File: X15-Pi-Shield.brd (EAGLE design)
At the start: 100 x 80 mm, 76 parts, among them J1 T2I, J2 T2I, J3 DF13-4P-1.25DSA, J4 T2I, J5 DF13-4P-1.25DSA, J6 DF13-4P-1.25DSA, Q1 220mA/50V/3.5Ω, Q2 2.5A/30V/105mΩ, Q3 220mA/50V/3.5Ω, Q4 220mA/50V/3.5Ω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

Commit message: 2nd try
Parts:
- removed C8: 150uF, CAP, Tantalum 150 uF - Kemet 2917 T491:2917(7343-31-METRIC)
- added C14: 150uF, X15-Pi-Shield-Parts:2917(7343-31-METRIC)
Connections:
- net GND: now also C14.-; no longer C8.-
- net PI_POWER: now also C14.+; no longer C8.+
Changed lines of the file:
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@@
 <attribute name="VALUE" x="-17.78" y="-386.842" size="0.6096" layer="27" font="vector" ratio="20" align="top-center"/>
-</element>
-<element name="C8" library="CAP, Tantalum 150 uF - Kemet 2917 T491" package="2917(7343-31-METRIC)" package3d_urn="urn:adsk.eagle:package:25131320/3" value="150uF" x="-13.97" y="-392.43" smashed="yes">
-<attribute name="NAME" x="-13.97" y="-389.89" size="1.27" layer="25" align="bottom-center"/>
-<attribute name="VALUE" x="-13.97" y="-394.97" size="1.27" layer="27" align="top-center"/>
 </element>
 <element name="J3" library="X15-Pi-Shield-Parts" package="DF13-4P-1.25DSA" value="DF13-4P-1.25DSA" x="-25.4" y="-391.16" smashed="yes">
@@
 <attribute name="VALUE" x="-76.2" y="-550.672" size="0.6096" layer="27" font="vector" ratio="20" align="top-center"/>
 </element>
+<element name="C14" library="X15-Pi-Shield-Parts" package="2917(7343-31-METRIC)" package3d_urn="urn:adsk.eagle:package:25131320/3" value="150uF" x="-72.39" y="-556.26" smashed="yes">
+<attribute name="NAME" x="-72.39" y="-553.72" size="1.27" layer="25" align="bottom-center"/>
+<attribute name="VALUE" x="-72.39" y="-558.8" size="1.27" layer="27" align="top-center"/>
+</element>
 </elements>
 <signals>
@@
 <contactref element="U$5" pad="GND"/>
 <contactref element="C7" pad="2"/>
-<contactref element="C8" pad="-"/>
 <contactref element="J3" pad="4"/>
 <contactref element="J5" pad="4"/>
@@
 <contactref element="U$6" pad="6"/>
 <contactref element="U$6" pad="10"/>
-<contactref element="C9" pad="-"/>
-<contactref element="U1" pad="8"/>
 <contactref element="D4" pad="C"/>
 <contactref element="D3" pad="C"/>
@@
 <contactref element="J15" pad="1"/>
 <contactref element="D5" pad="C"/>
-<contactref element="Q3" pad="2"/>
-<contactref element="U$7" pad="2"/>
 <contactref element="C10" pad="2"/>
 <contactref element="U$8" pad="11"/>
@@
 <contactref element="C12" pad="2"/>
 <contactref element="C13" pad="2"/>
+<contactref element="U1" pad="8"/>
+<contactref element="C9" pad="-"/>
+<contactref element="Q3" pad="2"/>
+<contactref element="U$7" pad="2"/>
+<contactref element="C14" pad="-"/>
 <wire x1="4.5466" y1="-262.4582" x2="12.1666" y2="-262.4582" width="0" layer="19" extent="1-1"/>
 <wire x1="-0.5334" y1="-264.9982" x2="4.5466" y2="-262.4582" width="0" layer="19" extent="1-1"/>
@@
 <wire x1="-6.985" y1="-361.95" x2="-6.35" y2="-337.82" width="0" layer="19" extent="1-1"/>
 <wire x1="-16.93" y1="-370.84" x2="-6.985" y2="-361.95" width="0" layer="19" extent="1-1"/>
-<wire x1="-10.75" y1="-392.43" x2="-16.93" y2="-370.84" width="0" layer="19" extent="1-1"/>
-<wire x1="-27.275" y1="-391.16" x2="-10.75" y2="-392.43" width="0" layer="19" extent="1-1"/>
+<wire x1="-27.275" y1="-391.16" x2="-16.93" y2="-370.84" width="0" layer="19" extent="1-1"/>
 <wire x1="-36.165" y1="-391.16" x2="-27.275" y2="-391.16" width="0" layer="19" extent="1-1"/>
 <wire x1="-45.055" y1="-391.16" x2="-36.165" y2="-391.16" width="0" layer="19" extent="1-1"/>
@@
 <wire x1="-75.35" y1="-518.16" x2="-71.4756" y2="-512.7498" width="0" layer="19" extent="1-1"/>
 <wire x1="-75.35" y1="-549.91" x2="-75.35" y2="-518.16" width="0" layer="19" extent="1-1"/>
+<wire x1="-69.17" y1="-556.26" x2="-75.35" y2="-549.91" width="0" layer="19" extent="1-1"/>
 <wire x1="-4.95" y1="-181.35" x2="-5.6134" y2="-262.4582" width="0" layer="19" extent="1-1"/>
 <wire x1="-19.05" y1="-166.37" x2="-4.95" y2="-181.35" width="0" layer="19" extent="1-1"/>
@@
 <contactref element="U$4" pad="2"/>
 <contactref element="R14" pad="2"/>
-<contactref element="C8" pad="+"/>
 <contactref element="R13" pad="2"/>
-<wire x1="-16.93" y1="-386.08" x2="-17.19" y2="-392.43" width="0" layer="19" extent="1-1"/>
+<contactref element="C14" pad="+"/>
 <wire x1="-16.93" y1="-382.27" x2="-16.93" y2="-386.08" width="0" layer="19" extent="1-1"/>
 <wire x1="-10.6934" y1="-262.4582" x2="-16.93" y2="-382.27" width="0" layer="19" extent="1-1"/>
 <wire x1="-8.1534" y1="-262.4582" x2="-10.6934" y2="-262.4582" width="0" layer="19" extent="1-1"/>
+<wire x1="-75.61" y1="-556.26" x2="-16.93" y2="-386.08" width="0" layer="19" extent="1-1"/>
 </signal>
 <signal name="SCL/3.6C">

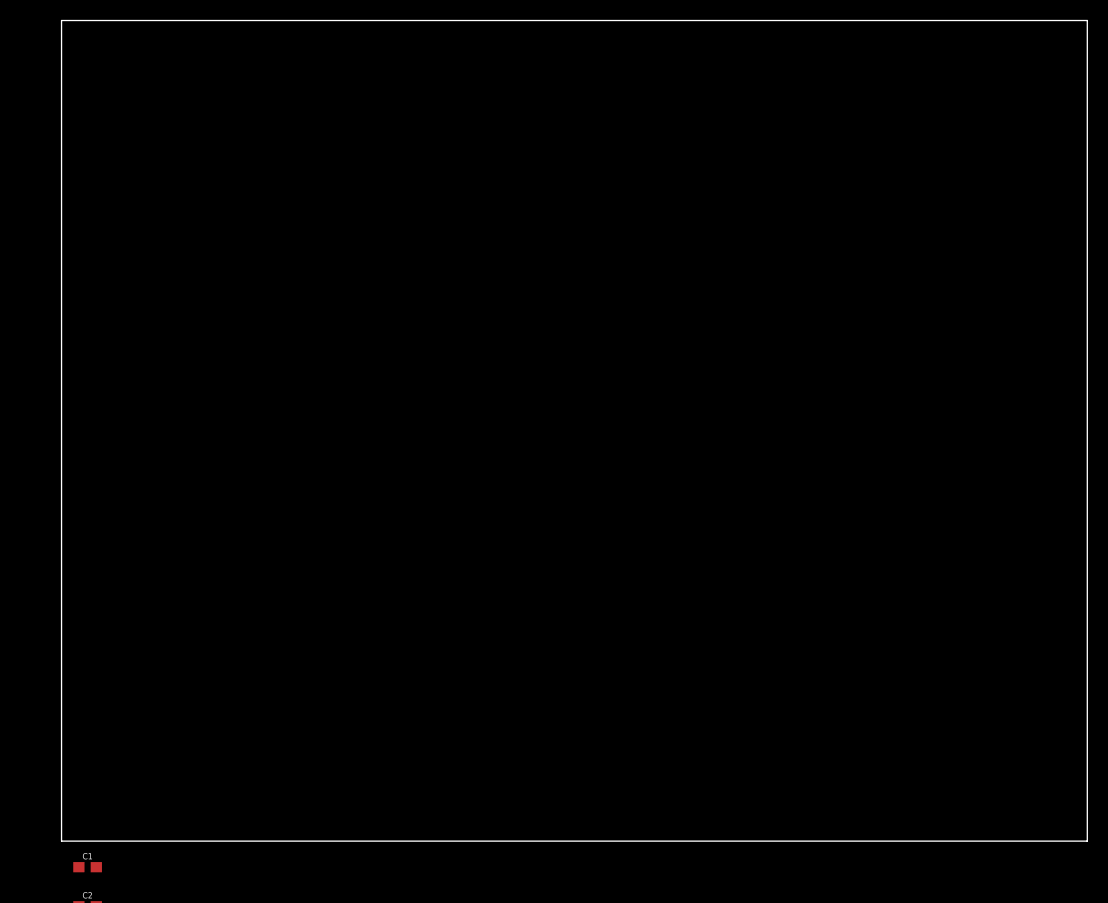
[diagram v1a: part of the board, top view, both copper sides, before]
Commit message: Board Dimensions
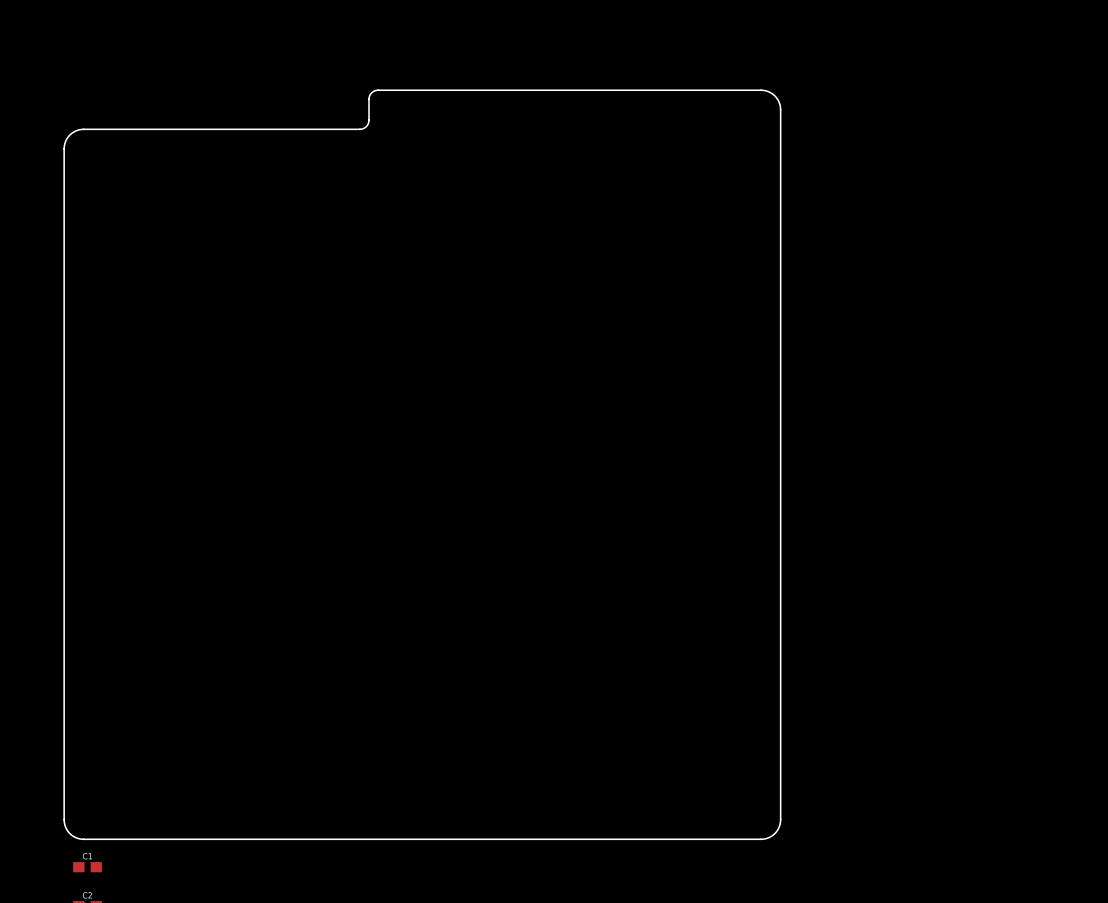
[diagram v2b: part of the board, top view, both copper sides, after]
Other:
- board size 100 x 80 mm -> 69.8 x 73 mm
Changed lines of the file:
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@@
 <setting verticaltext="up"/>
 </settings>
-<grid distance="50" unitdist="mil" unit="mil" style="lines" multiple="1" display="no" altdistance="5" altunitdist="mil" altunit="mil"/>
+<grid distance="1" unitdist="mil" unit="mil" style="lines" multiple="1" display="no" altdistance="5" altunitdist="mil" altunit="mil"/>
 <layers>
 <layer number="1" name="Top" color="4" fill="1" visible="yes" active="yes"/>
@@
 <layer number="154" name="FabDoc2" color="7" fill="1" visible="yes" active="yes"/>
 <layer number="155" name="FabDoc3" color="7" fill="1" visible="yes" active="yes"/>
+<layer number="166" name="AntennaArea" color="7" fill="1" visible="yes" active="yes"/>
+<layer number="168" name="4mmHeightArea" color="7" fill="1" visible="yes" active="yes"/>
 <layer number="191" name="mNets" color="7" fill="1" visible="yes" active="yes"/>
 <layer number="192" name="mBusses" color="7" fill="1" visible="yes" active="yes"/>
@@
 <board>
 <plain>
-<wire x1="0" y1="0" x2="100" y2="0" width="0" layer="20"/>
-<wire x1="100" y1="0" x2="100" y2="80" width="0" layer="20"/>
-<wire x1="100" y1="80" x2="0" y2="80" width="0" layer="20"/>
-<wire x1="0" y1="80" x2="0" y2="0" width="0" layer="20"/>
+<wire x1="2.159" y1="69.3928" x2="29.083" y2="69.3928" width="0.1524" layer="20"/>
+<wire x1="29.083" y1="69.3928" x2="29.972" y2="70.2818" width="0.1524" layer="20" curve="90"/>
+<wire x1="29.972" y1="70.2818" x2="29.972" y2="72.3138" width="0.1524" layer="20"/>
+<wire x1="29.972" y1="72.3138" x2="30.861" y2="73.2028" width="0.1524" layer="20" curve="-90"/>
+<wire x1="30.861" y1="73.2028" x2="68.199" y2="73.2028" width="0.1524" layer="20"/>
+<wire x1="68.199" y1="73.2028" x2="70.104" y2="71.2978" width="0.1524" layer="20" curve="-90"/>
+<wire x1="70.104" y1="71.2978" x2="70.104" y2="2.0828" width="0.1524" layer="20"/>
+<wire x1="70.104" y1="2.0828" x2="68.199" y2="0.1778" width="0.1524" layer="20" curve="-90"/>
+<wire x1="68.199" y1="0.1778" x2="2.159" y2="0.1778" width="0.1524" layer="20"/>
+<wire x1="2.159" y1="0.1778" x2="0.254" y2="2.0828" width="0.1524" layer="20" curve="-90"/>
+<wire x1="0.254" y1="2.0828" x2="0.254" y2="67.4878" width="0.1524" layer="20"/>
+<wire x1="0.254" y1="67.4878" x2="2.159" y2="69.3928" width="0.1524" layer="20" curve="-90"/>
 </plain>
 <attributes>
